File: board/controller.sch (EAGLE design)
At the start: 61 parts, among them J1 X_SIG, J10 COOLANT, J12 VIN, J13 GND, J15 A_SIG, J16 +5V, J17 PROBE, J18 FEED_OVERRIDE, J19 MOTOR_CURRENT, J2 Y_SIG, J20 WHEEL, J22 DISPLAY, J23 ERROR, J24 HOLDING, J25 SPINDLE, J26 SD_READER, J3 Z_SIG, J4 RESET, J5 Z_DISPLAY, J6 FEED_HOLD, J8 CYCLE_START, U5 SENSOR-IR-THRU

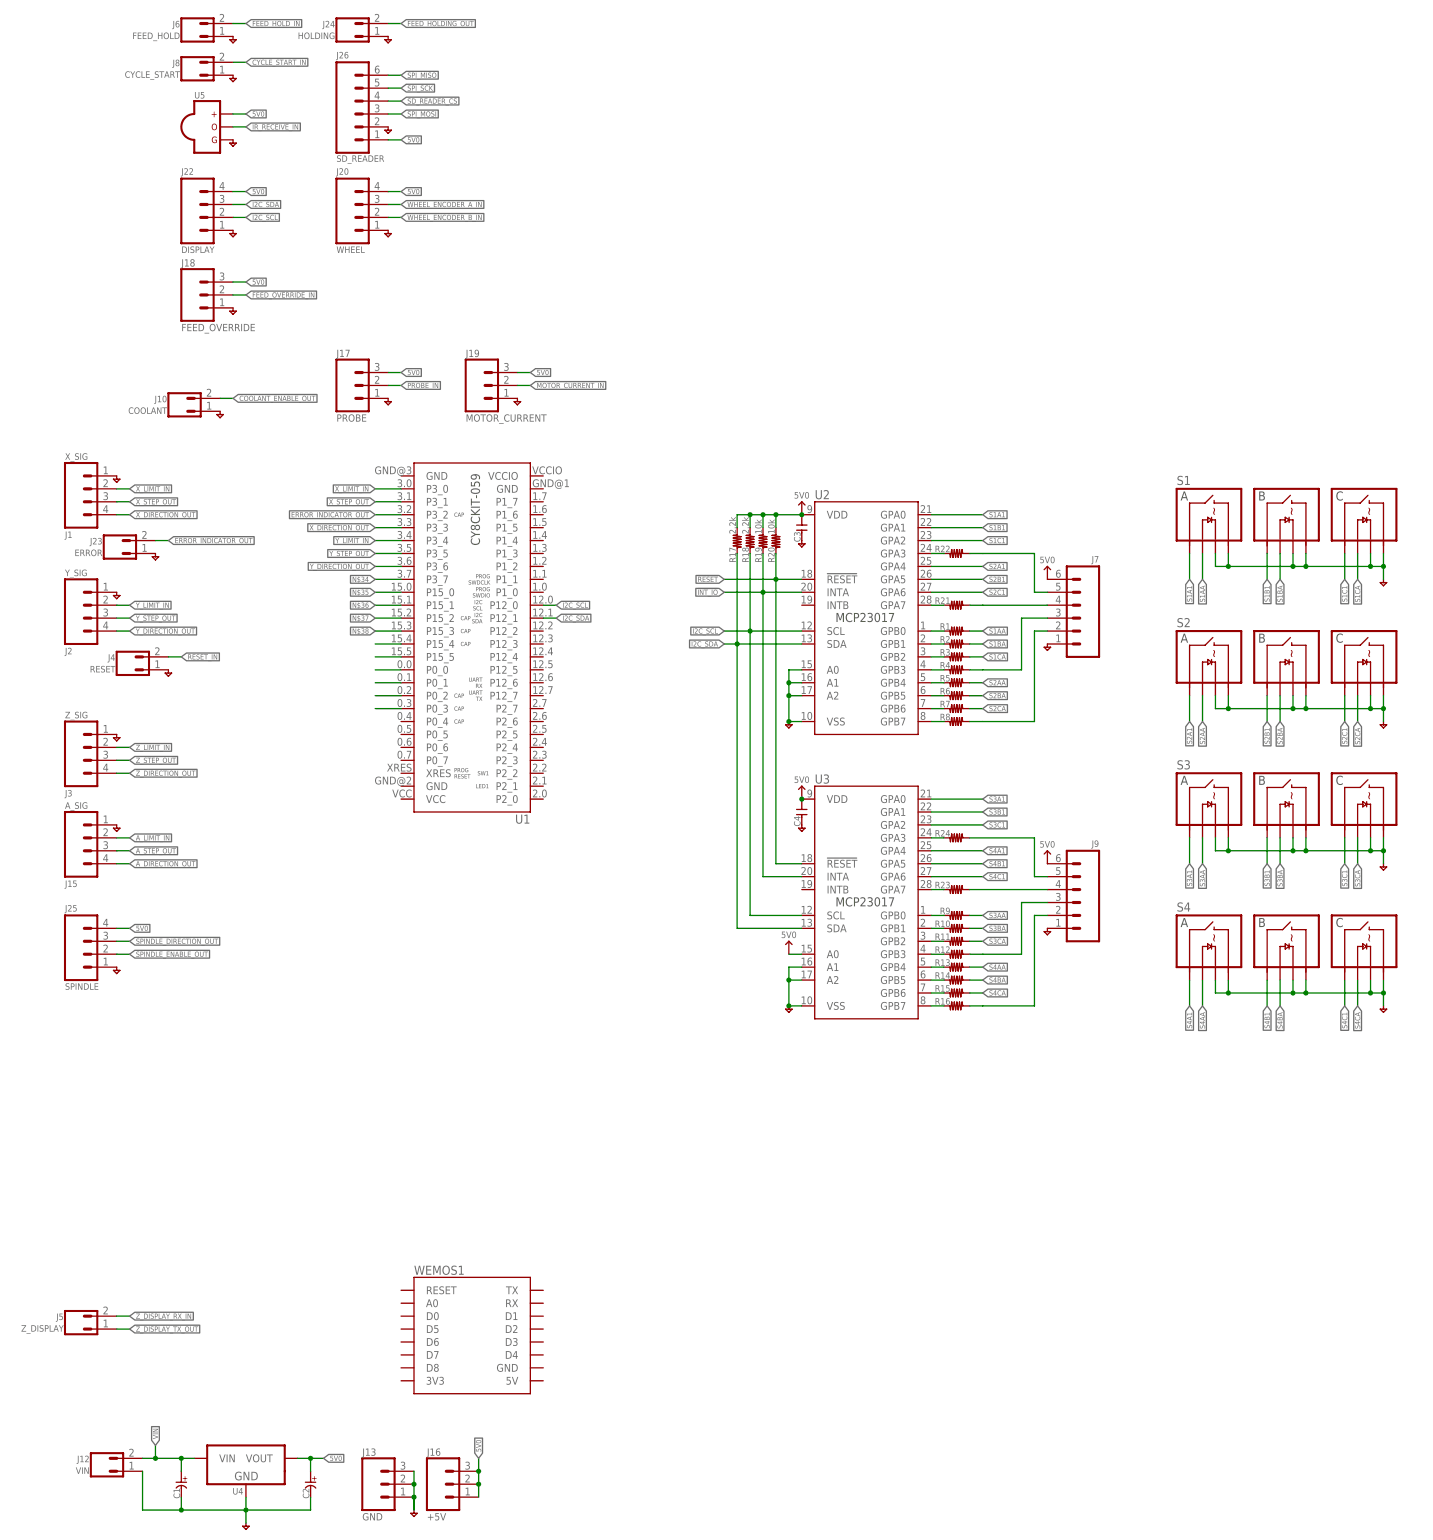
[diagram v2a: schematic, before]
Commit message: pin assignment and routing near completion
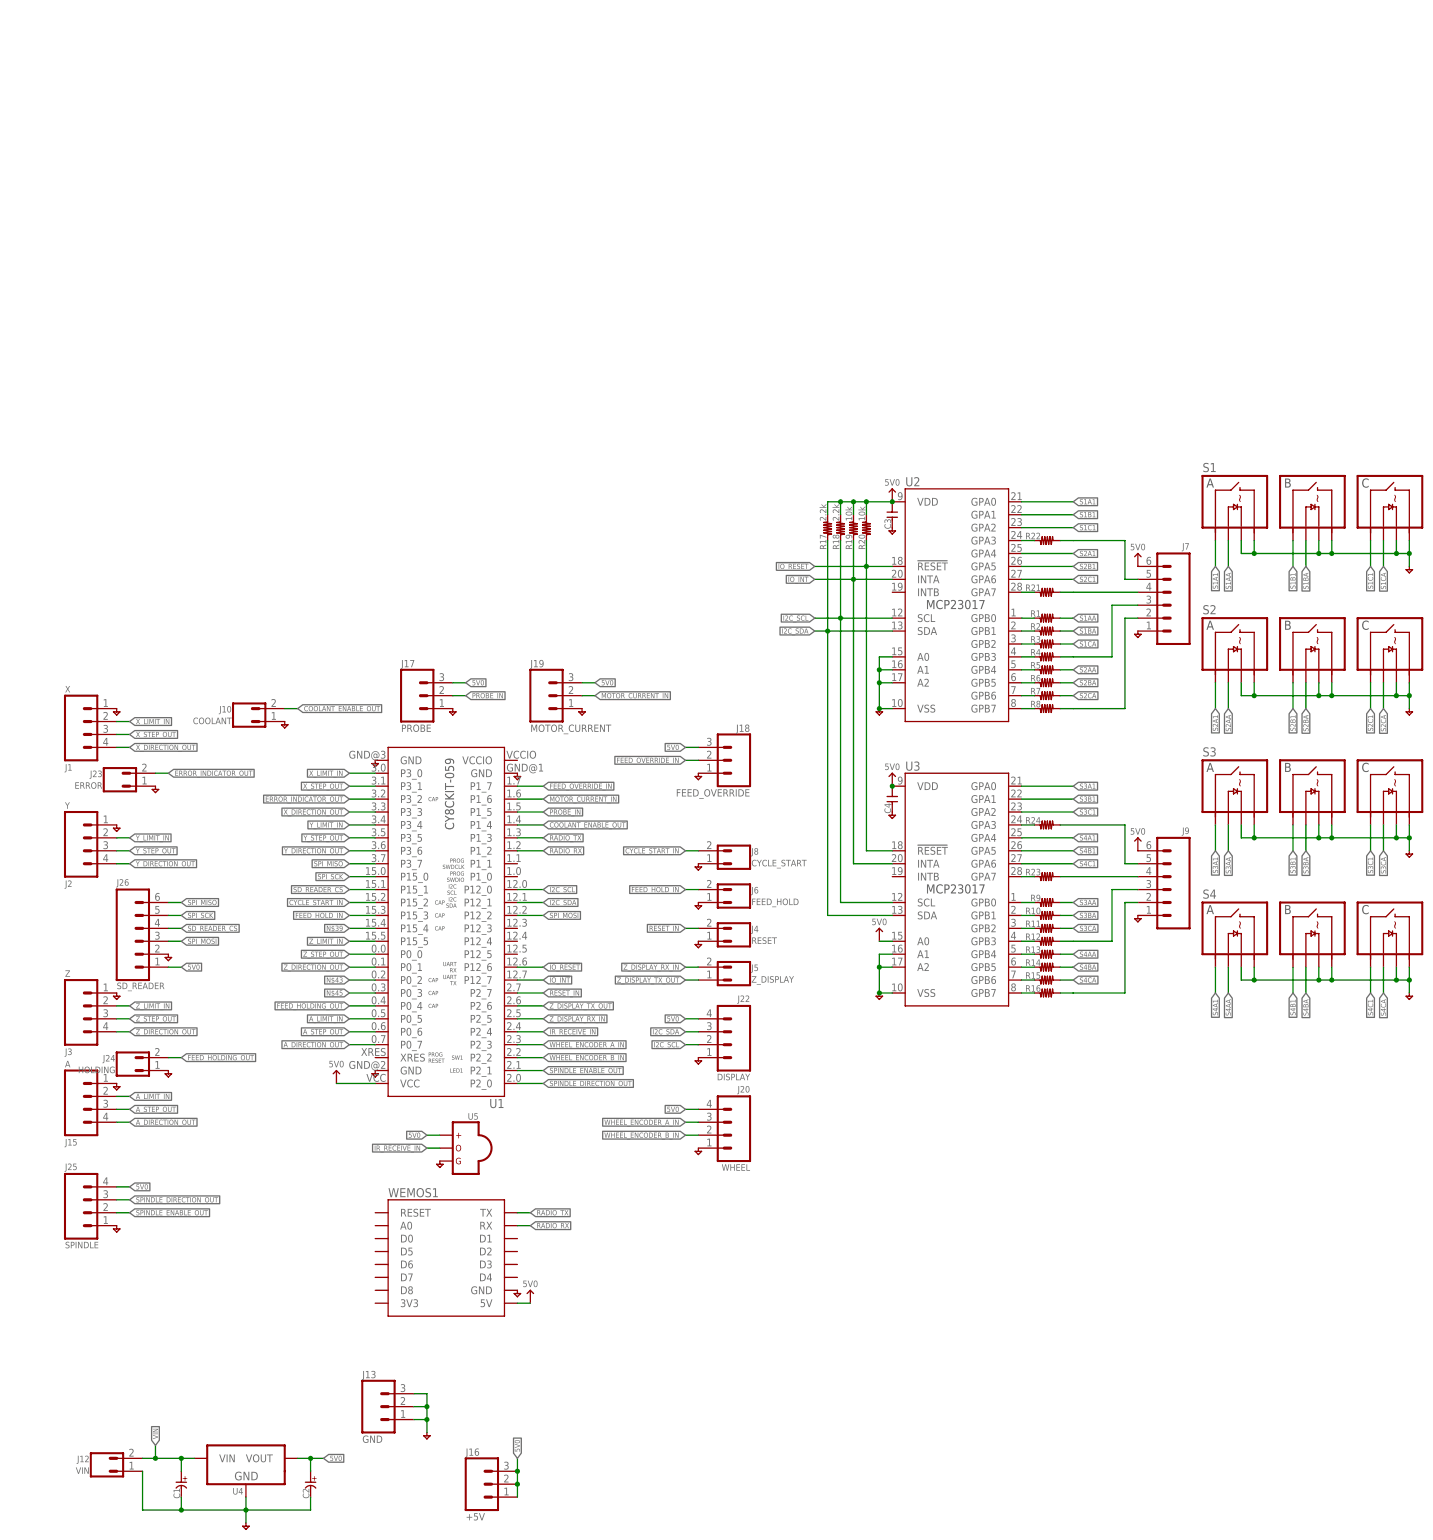
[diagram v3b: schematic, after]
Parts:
- J1: value X_SIG -> X
- J15: value A_SIG -> A
- J2: value Y_SIG -> Y
- J3: value Z_SIG -> Z
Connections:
- removed net !INT_IO: R19.1, U2.INTA, U3.INTA
- removed net !RESET: R20.1, U2.!RESET, U3.!RESET
- removed net N$34: U1.P3_7
- removed net N$35: U1.P15_0
- removed net N$36: U1.P15_1
- removed net N$37: U1.P15_2
- removed net N$38: U1.P15_3
- removed net N$40: U1.P15_5
- removed net N$41: U1.P0_0
- removed net N$42: U1.P0_1
- new net !IO_INT: R19.1, U1.P12_7, U2.INTA, U3.INTA
- new net !IO_RESET: R20.1, U1.P12_6, U2.!RESET, U3.!RESET
- new net RADIO_RX: U1.P1_2, WEMOS1.RX
- new net RADIO_TX: U1.P1_3, WEMOS1.TX
- net 5V0: now also U1.VCC, WEMOS1.5V
- net A_DIRECTION_OUT: now also U1.P0_7
- net A_LIMIT_IN: now also U1.P0_5
- net A_STEP_OUT: now also U1.P0_6
- net COOLANT_ENABLE_OUT: now also U1.P1_4
- net CYCLE_START_IN: now also U1.P15_2
- net FEED_HOLDING_OUT: now also U1.P0_4
- net FEED_HOLD_IN: now also U1.P15_3
- net FEED_OVERRIDE_IN: now also U1.P1_7
- net GND: now also U1.GND@1, U1.GND@2, U1.GND@3, WEMOS1.GND
- net IR_RECEIVE_IN: now also U1.P2_4
- net MOTOR_CURRENT_IN: now also U1.P1_6
- net PROBE_IN: now also U1.P1_5
- net RESET_IN: now also U1.P2_7
- net SD_READER_CS: now also U1.P15_1
- net SPINDLE_DIRECTION_OUT: now also U1.P2_0
- net SPINDLE_ENABLE_OUT: now also U1.P2_1
- net SPI_MISO: now also U1.P3_7
- net SPI_MOSI: now also U1.P12_2
- net SPI_SCK: now also U1.P15_0
- net WHEEL_ENCODER_A_IN: now also U1.P2_3
- net WHEEL_ENCODER_B_IN: now also U1.P2_2
- net Z_DIRECTION_OUT: now also U1.P0_1
- net Z_DISPLAY_RX_IN: now also U1.P2_5
- net Z_DISPLAY_TX_OUT: now also U1.P2_6
- net Z_LIMIT_IN: now also U1.P15_5
- net Z_STEP_OUT: now also U1.P0_0
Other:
- moved on the sheet: C3, C4, J1, J10, J13, J15, J16, J17, J18, J19, J2, J20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

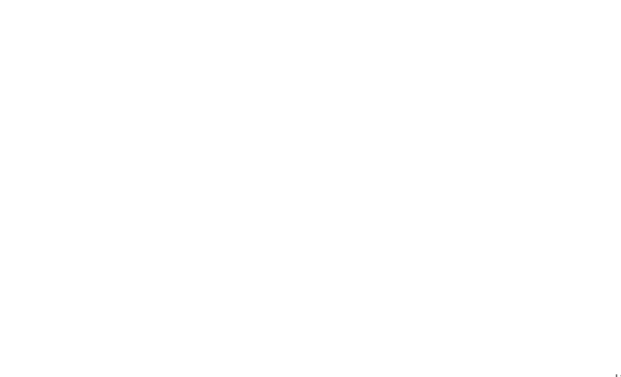
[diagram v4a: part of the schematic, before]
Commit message: corrected keyboard switch dimensions
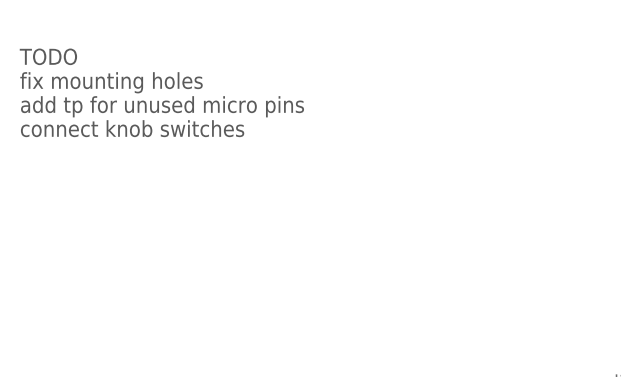
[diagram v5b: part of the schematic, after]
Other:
- note added: "TODO fix mounting holes add tp for unused micro pins connect knob switches"
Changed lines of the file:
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@@
 <sheet>
 <plain>
+<text x="7.62" y="208.28" size="1.778" layer="97" align="top-left">TODO
+fix mounting holes
+add tp for unused micro pins
+connect knob switches</text>
 </plain>
 <instances>

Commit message: finished routing, almost ready to send
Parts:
- removed J25: SPINDLE, holla:CONN-04-3.81MM-PLUGIN-SCREW
- added C5: 47u, holla:C-POLARIZED-E5-10
- added FID1, FID2: FIDUCIAL1.5X3, holla:FIDUCIAL1.5X3
- added GND: (no value), holla:TESTPOINTTHRU
- added J11: SD_READER, holla:CONN-06-0.1
- added J14: GND, holla:CONN-03-3.81MM-PLUGIN-SCREW
- added J21: (no value), holla:CONN-06-.100-VERT-HEADER
- added R25, R26: (no value), holla:R-0603
- C1, C2: device holla:C-POLARIZED-E5-10 -> holla:C-0603
- C3: value (none) -> 1u
- C4: value (none) -> 47u; device holla:C-0603 -> holla:C-POLARIZED-E5-10
- J1: value X -> COOLANT; device holla:CONN-04-3.81MM-PLUGIN-SCREW -> holla:CONN-02-3.81MM-PLUGIN-SCREW
- J10: value COOLANT -> FEED_HOLD; device holla:CONN-02-3.81MM-PLUGIN-SCREW -> holla:CONN-02-.100-VERT-HEADER
- J12: value VIN -> RESET; device holla:CONN-02-3.81MM-PLUGIN-SCREW -> holla:CONN-02-.100-VERT-HEADER
- J13: value GND -> Z; device holla:CONN-03-3.81MM-PLUGIN-SCREW -> holla:CONN-04-3.81MM-PLUGIN-SCREW
- J15: value A -> Z_DISPLAY; device holla:CONN-04-3.81MM-PLUGIN-SCREW -> holla:CONN-02-3.81MM-PLUGIN-SCREW
- J16: value +5V -> (none); device holla:CONN-03-3.81MM-PLUGIN-SCREW -> holla:CONN-05-.100-VERT-HEADER
- J17: value PROBE -> (none); device holla:CONN-03-3.81MM-PLUGIN-SCREW -> holla:CONN-02-0.1
- J18: value FEED_OVERRIDE -> DISPLAY; device holla:CONN-03-.100-VERT-HEADER -> holla:CONN-04-.100-VERT-HEADER
- J19: value MOTOR_CURRENT -> A; device holla:CONN-03-3.81MM-PLUGIN-SCREW -> holla:CONN-04-3.81MM-PLUGIN-SCREW
- J2: value Y -> PROBE; device holla:CONN-04-3.81MM-PLUGIN-SCREW -> holla:CONN-03-3.81MM-PLUGIN-SCREW
- J20: value WHEEL -> HOLDING; device holla:CONN-04-.100-VERT-HEADER -> holla:CONN-02-.100-VERT-HEADER
- J22: value DISPLAY -> WHEEL
- J23: value ERROR -> SPINDLE; device holla:CONN-02-.100-VERT-HEADER -> holla:CONN-04-3.81MM-PLUGIN-SCREW
- J24: value HOLDING -> +5V; device holla:CONN-02-.100-VERT-HEADER -> holla:CONN-03-3.81MM-PLUGIN-SCREW
- J26: value SD_READER -> GND; device holla:CONN-06-0.1 -> holla:CONN-03-3.81MM-PLUGIN-SCREW
- J3: value Z -> MOTOR_CURRENT; device holla:CONN-04-3.81MM-PLUGIN-SCREW -> holla:CONN-03-3.81MM-PLUGIN-SCREW
- J4: value RESET -> X; device holla:CONN-02-.100-VERT-HEADER -> holla:CONN-04-3.81MM-PLUGIN-SCREW
- J5: value Z_DISPLAY -> (none); device holla:CONN-02-3.81MM-PLUGIN-SCREW -> holla:CONN-06-.100-VERT-HEADER
- J6: value FEED_HOLD -> ERROR
- J7: device holla:CONN-06-.100-VERT-HEADER -> holla:CONN-05-PTH
- J9: value (none) -> Y; device holla:CONN-06-.100-VERT-HEADER -> holla:CONN-04-3.81MM-PLUGIN-SCREW
- R17, R18: value 2.2k -> (none)
- R19, R20: value 10k -> (none)
- R2, R5: value (none) -> 2.2k
- R22, R23: value (none) -> 10k
- U1: device holla:BOARD-PSOC-CY8CKIT-059 -> holla:IO-MCP23017SO
- U2: device holla:IO-MCP23017SO -> holla:BOARD-PSOC-CY8CKIT-059
- renumbered S1 to S103, S2 to S102, S3 to S101, S4 to S100, U5 to U100
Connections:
- removed net N$39: U1.P15_4
- new net FEED_OVERRIDE_BTN: J7.5, U2.P1_0
- new net FEED_OVERRIDE_OFF: J7.4, U2.P1_1
- new net P12.3: J16.4, U2.P12_3
- new net P12.4: J16.3, U2.P12_4
- new net P12.5: J16.2, U2.P12_5
- new net VIN_SCALE: C3.1, R16.2, R18.1, U2.P1_4
- net !IO_INT: now also R23.1, U1.INTA, U2.P12_7; no longer R19.1, U1.P12_7, U2.INTA
- net !IO_RESET: now also R22.1, U1.!RESET, U2.P12_6; no longer R20.1, U1.P12_6, U2.!RESET
- net 5V0: now also C1.1, C2.1, C4.+, J11.1, J16.5, J18.2, J2.3, J21.6, J23.4, J24.1, J24.2, J24.3, J3.3, J5.6, J7.3, R2.2, R22.2, R23.2, R5.2, U1.VDD, U2.VCC; no longer C2.+, C3.1, C4.1, J16.1, J16.2, J16.3, J17.3, J18.3, J19.3, J20.4, J25.4, J26.1, J7.6, J9.6, R17.2, R18.2, R19.2, R20.2, U1.VCC, U2.VDD
- net A_DIRECTION_OUT: now also J19.4, U2.P0_7; no longer J15.4, U1.P0_7
- net A_LIMIT_IN: now also J19.2, U2.P0_5; no longer J15.2, U1.P0_5
- net A_STEP_OUT: now also J19.3, U2.P0_6; no longer J15.3, U1.P0_6
- net COOLANT_ENABLE_OUT: now also J1.2, U2.P15_4; no longer J10.2, U1.P1_4
- net CYCLE_START_IN: now also U2.P15_2; no longer U1.P15_2
- net ERROR_INDICATOR_OUT: now also J6.2, U2.P3_2; no longer J23.2, U1.P3_2
- net FEED_HOLDING_OUT: now also J20.2, U2.P0_4; no longer J24.2, U1.P0_4
- net FEED_HOLD_IN: now also J10.2, U2.P15_3; no longer J6.2, U1.P15_3
- net FEED_OVERRIDE_IN: now also J7.2, U2.P1_7; no longer J18.2, U1.P1_7
- net GND: now also C1.2, C2.2, C4.-, C5.-, GND.P$1, J11.2, J14.1, J14.2, J14.3, J16.1, J21.1, J26.1, J5.1, R16.1, U1.A0, U1.A1, U1.A2, U1.VSS, U2.GND@1, U2.GND@2, U2.GND@3; no longer C1.-, C2.-, C4.2, J13.2, J13.3, J15.1, J17.1, J24.1, J25.1, J26.2, U1.GND@1, U1.GND@2, U1.GND@3, U2.A0, U2.A1, U2.A2, U2.VSS
- net I2C_SCL: now also J18.4, R2.1, U1.SCL, U2.P12_0; no longer J22.2, R18.1, U1.P12_0, U2.SCL
- net I2C_SDA: now also J18.3, R5.1, U1.SDA, U2.P12_1; no longer J22.3, R17.1, U1.P12_1, U2.SDA
- net IR_RECEIVE_IN: now also U2.P2_4; no longer U1.P2_4
- net MOTOR_CURRENT_IN: now also J3.2, U2.P1_6; no longer J19.2, U1.P1_6
- net N$1: now also R4.1, U1.GPB0; no longer R1.1, U2.GPB0
- net N$10: now also J21.5, R21.2; no longer J9.5, R24.2
- net N$11: now also J21.4, R20.2; no longer J9.4, R23.2
- net N$15: now also U1.GPB2; no longer U2.GPB2
- net N$16: now also R7.1, U1.GPB3; no longer R4.1, U2.GPB3
- net N$17: now also R12.1, U1.GPB4; no longer R5.1, U2.GPB4
- net N$18: now also R11.1, U1.GPB5; no longer R6.1, U2.GPB5
- net N$19: now also R10.1, U1.GPB6; no longer R7.1, U2.GPB6
- net N$2: now also R1.1, U1.GPB1; no longer R2.1, U2.GPB1
- net N$20: now also R6.1, U1.GPB7; no longer R8.1, U2.GPB7
- net N$21: now also R15.1; no longer R9.1
- net N$22: now also R14.1; no longer R10.1
- net N$23: now also R13.1; no longer R11.1
- net N$24: now also R19.1; no longer R12.1
- net N$25: now also R26.1; no longer R13.1
- net N$26: now also R25.1; no longer R14.1
- net N$27: now also R24.1; no longer R15.1
- net N$28: now also R17.1; no longer R16.1
- net N$3: now also R9.1, U1.GPA3; no longer R22.1, U2.GPA3
- net N$30: now also J5.2, R6.2; no longer J7.2, R8.2
- net N$4: now also J5.5, R9.2; no longer J7.5, R22.2
- net N$43: now also J17.2, U2.P0_2; no longer U1.P0_2
- net N$44: now also J21.3, R19.2; no longer J9.3, R12.2
- net N$45: now also J17.1, U2.P0_3; no longer U1.P0_3
- net N$48: now also J21.2, R17.2; no longer J9.2, R16.2
- net N$5: now also R8.1, U1.GPA7; no longer R21.1, U2.GPA7
- net N$6: now also J5.3, R7.2; no longer J7.3, R4.2
- net N$7: now also J5.4, R8.2; no longer J7.4, R21.2
- net N$8: now also R21.1; no longer R24.1
- net N$9: now also R20.1; no longer R23.1
- net PROBE_IN: now also J2.2, U2.P1_5; no longer J17.2, U1.P1_5
- net RADIO_RX: now also U2.P1_2; no longer U1.P1_2
- net RADIO_TX: now also U2.P1_3; no longer U1.P1_3
- net RESET_IN: now also J12.2, U2.P2_7; no longer J4.2, U1.P2_7
- net S1A1: now also U1.GPA0; no longer U2.GPA0
- net S1AA: now also R4.2; no longer R1.2
- net S1B1: now also U1.GPA1; no longer U2.GPA1
- net S1BA: now also R1.2; no longer R2.2
- net S1C1: now also U1.GPA2; no longer U2.GPA2
- net S2A1: now also U1.GPA4; no longer U2.GPA4
- net S2AA: now also R12.2; no longer R5.2
- net S2B1: now also U1.GPA5; no longer U2.GPA5
- net S2BA: now also R11.2; no longer R6.2
- net S2C1: now also U1.GPA6; no longer U2.GPA6
- net S2CA: now also R10.2; no longer R7.2
- net S3AA: now also R15.2; no longer R9.2
- net S3BA: now also R14.2; no longer R10.2
- net S3CA: now also R13.2; no longer R11.2
- net S4AA: now also R26.2; no longer R13.2
- net S4BA: now also R25.2; no longer R14.2
- net S4CA: now also R24.2; no longer R15.2
- net SD_READER_CS: now also J11.4, U2.P15_1; no longer J26.4, U1.P15_1
- net SPINDLE_DIRECTION_OUT: now also J23.3, U2.P2_0; no longer J25.3, U1.P2_0
- net SPINDLE_ENABLE_OUT: now also J23.2, U2.P2_1; no longer J25.2, U1.P2_1
- net SPI_MISO: now also J11.6, U2.P3_7; no longer J26.6, U1.P3_7
- net SPI_MOSI: now also J11.3, U2.P12_2; no longer J26.3, U1.P12_2
- net SPI_SCK: now also J11.5, U2.P15_0; no longer J26.5, U1.P15_0
- net VIN: now also C5.+, J26.2, J26.3, R18.2; no longer C1.+, J12.2
- net WHEEL_ENCODER_A_IN: now also J22.3, U2.P2_3; no longer J20.3, U1.P2_3
- net WHEEL_ENCODER_B_IN: now also J22.2, U2.P2_2; no longer J20.2, U1.P2_2
- net X_DIRECTION_OUT: now also J4.4, U2.P3_3; no longer J1.4, U1.P3_3
- net X_LIMIT_IN: now also J4.2, U2.P3_0; no longer J1.2, U1.P3_0
- net X_STEP_OUT: now also J4.3, U2.P3_1; no longer J1.3, U1.P3_1
- net Y_DIRECTION_OUT: now also J9.4, U2.P3_6; no longer J2.4, U1.P3_6
- net Y_LIMIT_IN: now also J9.2, U2.P3_4; no longer J2.2, U1.P3_4
- net Y_STEP_OUT: now also J9.3, U2.P3_5; no longer J2.3, U1.P3_5
- net Z_DIRECTION_OUT: now also J13.4, U2.P0_1; no longer J3.4, U1.P0_1
- net Z_DISPLAY_RX_IN: now also J15.2, U2.P2_5; no longer J5.2, U1.P2_5
- net Z_DISPLAY_TX_OUT: now also J15.1, U2.P2_6; no longer J5.1, U1.P2_6
- net Z_LIMIT_IN: now also J13.2, U2.P15_5; no longer J3.2, U1.P15_5
- net Z_STEP_OUT: now also J13.3, U2.P0_0; no longer J3.3, U1.P0_0
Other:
- note added: "180804"
- note added: "Hyatt Controller"
- note added: "v1.0"
- note removed: "TODO fix mounting holes add tp for unused micro pins connect knob switches"
- moved on the sheet: C3, J10, J12, J22, J6, R1, R10, R11, R12, R13, R14, R15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
